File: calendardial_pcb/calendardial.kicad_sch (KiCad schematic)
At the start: 16 parts, among them J1 01x40 FFC Socket, P1 USB_C_Plug_USB2.0, U1 ESP32-S3-WROOM-1-N8R2, U2 TPS61169DCKR, U3 AP2112K-3.3, U4 FT232RL

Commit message: e
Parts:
- removed C4, C5: 100nF, symbol Device:C
- removed U4: FT232RL, Package_SO:SSOP-28_5.3x10.2mm_P0.65mm, symbol Interface_USB:FT232RL
- added SW1: BOOT, symbol Switch:SW_Push
- added SW2: RESET, symbol Switch:SW_Push
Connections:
- net 3.3V: now also J1.5 (Pin_5), R2.1, R3.2, U1.2 (3V3)
- net GND: now also J1.34 (Pin_34), J1.4 (Pin_4), J1.40 (Pin_40), U1.1 (GND), U1.40 (GND), U1.41 (GND), SW1.1, SW2.2; no longer R2.1, R3.2
- net LED A: now also C2.1, D1.1 (K), J1.1 (Pin_1)
- net at U1.3 (EN): now also R3.1, SW2.1; no longer R2.2
- net at U1.27 (IO0): now also R2.2, SW1.2; no longer R3.1
- net D15: now reaches U1.10 (IO17)
- net D15: now also J1.31 (Pin_31)
- net SPI SCK: now reaches U1.11 (IO18)
- net SPI SCK: now also J1.10 (Pin_10)
- net D6: now reaches U1.12 (IO8)
- net D6: now also J1.22 (Pin_22)
- net at U1.13 (USB_D-): now also P1.A7 (D-)
- net at U1.14 (USB_D+): now also P1.A6 (D+)
- net D1: now reaches U1.15 (IO3)
- net D1: now also J1.17 (Pin_17)
- net D7: now reaches U1.17 (IO9)
- net D7: now also J1.23 (Pin_23)
- net D8: now reaches U1.18 (IO10)
- net D8: now also J1.24 (Pin_24)
- net D9: now reaches U1.19 (IO11)
- net D9: now also J1.25 (Pin_25)
- net D10: now reaches U1.20 (IO12)
- net D10: now also J1.26 (Pin_26)
- net D11: now reaches U1.21 (IO13)
- net D11: now also J1.27 (Pin_27)
- net D12: now reaches U1.22 (IO14)
- net D12: now also J1.28 (Pin_28)
- net PCLK: now reaches U1.23 (IO21)
- net PCLK: now also J1.12 (Pin_12)
- net at U1.24 (IO47): now also J1.6 (Pin_6)
- net SPI CS: now reaches U1.25 (IO48)
- net SPI CS: now also J1.11 (Pin_11)
- net HSYNC: now reaches U1.31 (IO38)
- net HSYNC: now also J1.15 (Pin_15)
- net SPI SDA: now reaches U1.35 (IO42)
- net SPI SDA: now also J1.9 (Pin_9)
- net GPIO44: now reaches U1.36 (RXD0)
- net GPIO44: now also J1.14 (Pin_14)
- net DE: now reaches U1.37 (TXD0)
- net DE: now also J1.13 (Pin_13)
- net D0: now reaches U1.38 (IO2)
- net D0: now also J1.16 (Pin_16)
- net D2: now reaches U1.4 (IO4)
- net D2: now also J1.18 (Pin_18)
- net D3: now reaches U1.5 (IO5)
- net D3: now also J1.19 (Pin_19)
- net D4: now reaches U1.6 (IO6)
- net D4: now also J1.20 (Pin_20)
- net D5: now reaches U1.7 (IO7)
- net D5: now also J1.21 (Pin_21)
- net D13: now reaches U1.8 (IO15)
- net D13: now also J1.29 (Pin_29)
- net D14: now reaches U1.9 (IO16)
- net D14: now also J1.30 (Pin_30)
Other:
- note added: "Buttons"
- note removed: "USB to Serial"
- moved on the sheet: U1

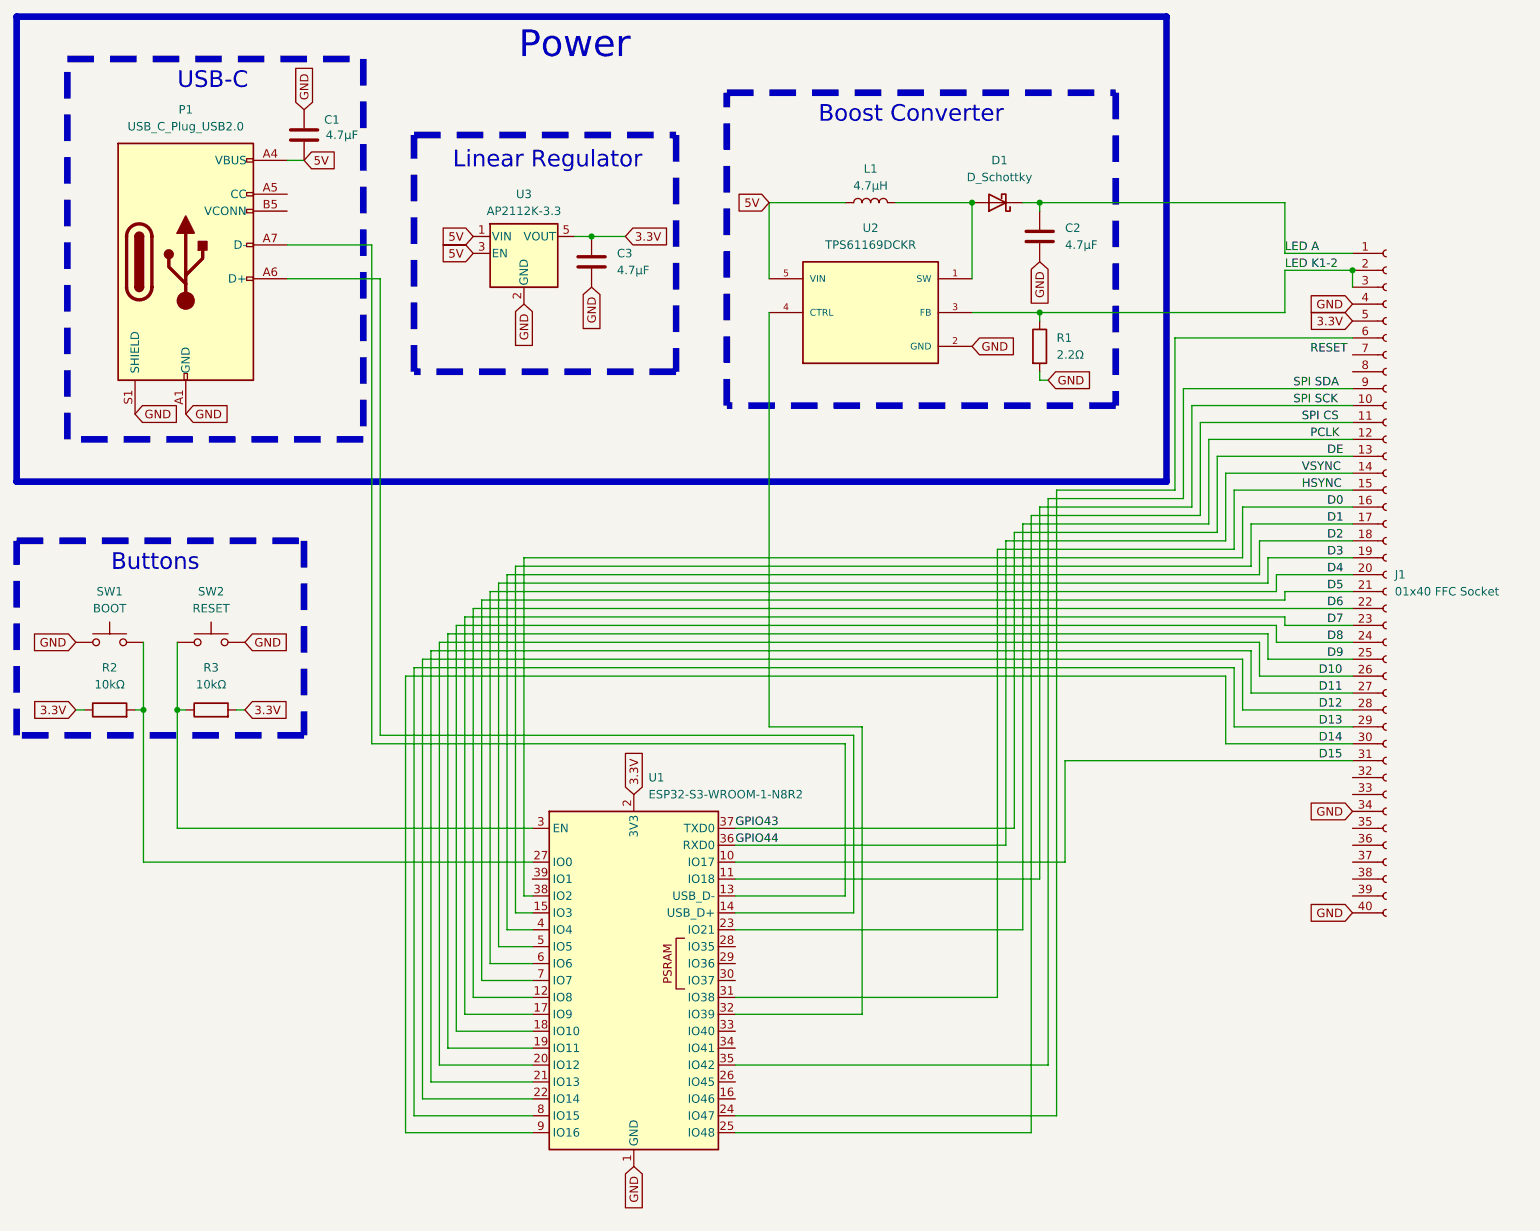
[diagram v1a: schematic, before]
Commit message: added setup for framebuf output p2
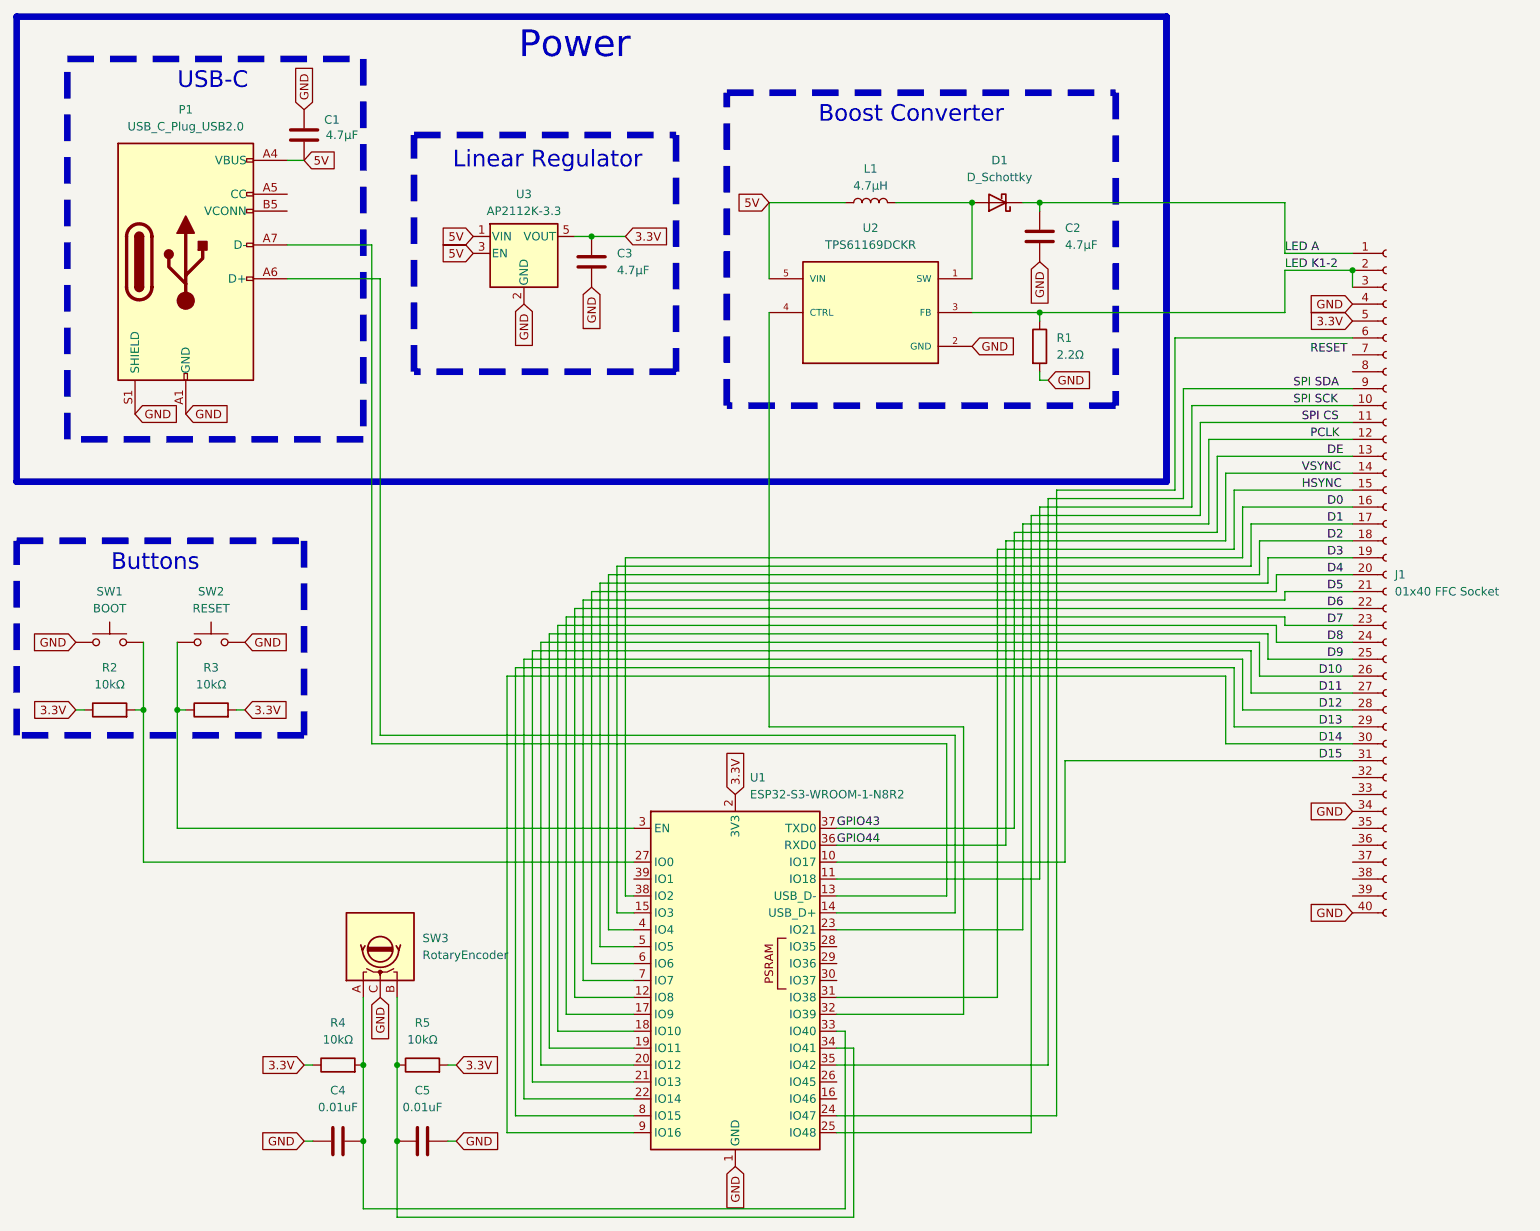
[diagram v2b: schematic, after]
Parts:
- added C4, C5: 0.01uF, symbol Device:C
- added R4, R5: 10kΩ, symbol Device:R
- added SW3: RotaryEncoder, symbol Device:RotaryEncoder
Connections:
- net 3.3V: now also R4.1, R5.2
- net GND: now also C4.1, C5.2, SW3.C
- net at U1.33 (IO40): now also C4.2, R4.2, SW3.A
- net at U1.34 (IO41): now also C5.1, R5.1, SW3.B
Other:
- moved on the sheet: U1
